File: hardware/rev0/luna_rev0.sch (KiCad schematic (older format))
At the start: 35 parts, among them J1 USB_B_Micro, J2 USB_B_Micro, J3 USB_A, J4 USB_B_Micro, J7 Conn_02x02_Counter_Clockwise, J8 Conn_Coaxial, J9 Conn_Coaxial, SW1 BTN_RECOVERY, SW2 BTN_DFU, SW3 BTN_RESET, U1 AP22814-SOT, U12 AP22814-SOT, Y1 DSC60xx

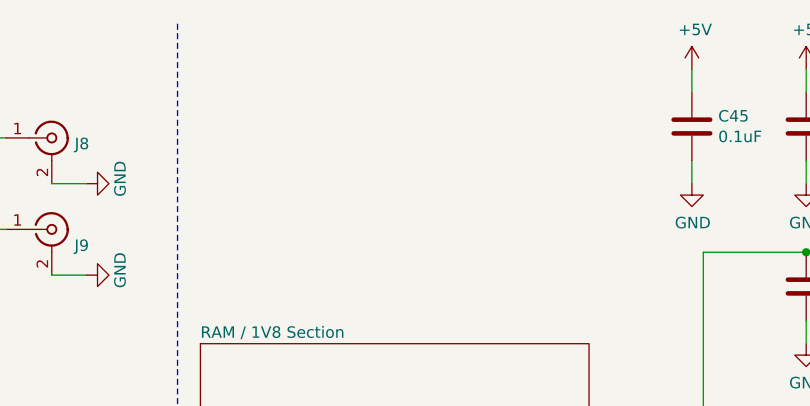
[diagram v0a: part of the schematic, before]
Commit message: hardware: add component selection notes
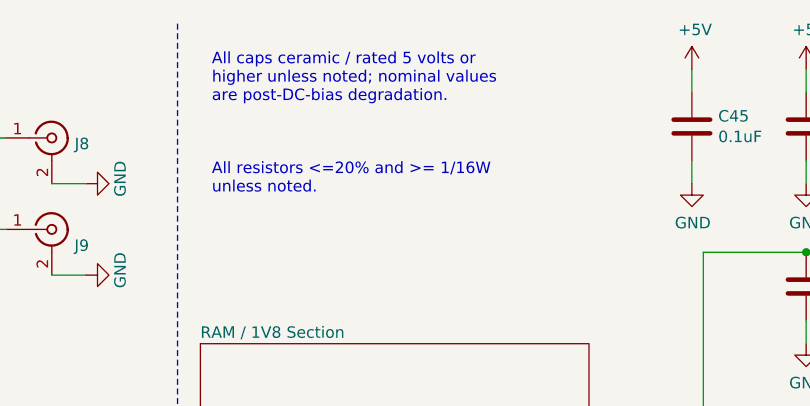
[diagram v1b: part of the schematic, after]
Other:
- note added: "All caps ceramic / rated 5 volts or\nhigher unless noted; nominal values\nare post-DC-bias degradation."
- note added: "All resistors <=20% and >= 1/16W\nunless noted."
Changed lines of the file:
@@
 Wire Wire Line
 	6150 700  6150 800
+Text Notes 4050 850  0    50   ~ 0
+All caps ceramic / rated 5 volts or\nhigher unless noted; nominal values\nare post-DC-bias degradation.
+Text Notes 4050 1250 0    50   ~ 0
+All resistors <=20% and >= 1/16W\nunless noted.
 $EndSCHEMATC

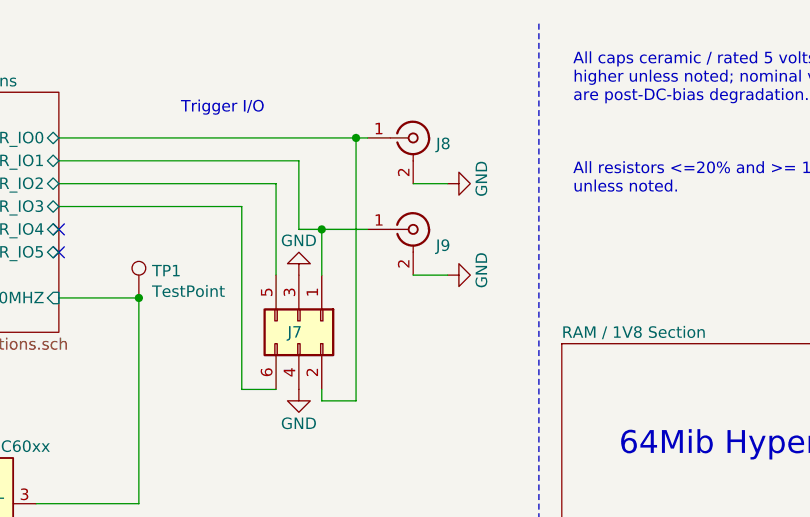
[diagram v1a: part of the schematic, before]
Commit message: hardware: do not populate J7-J9
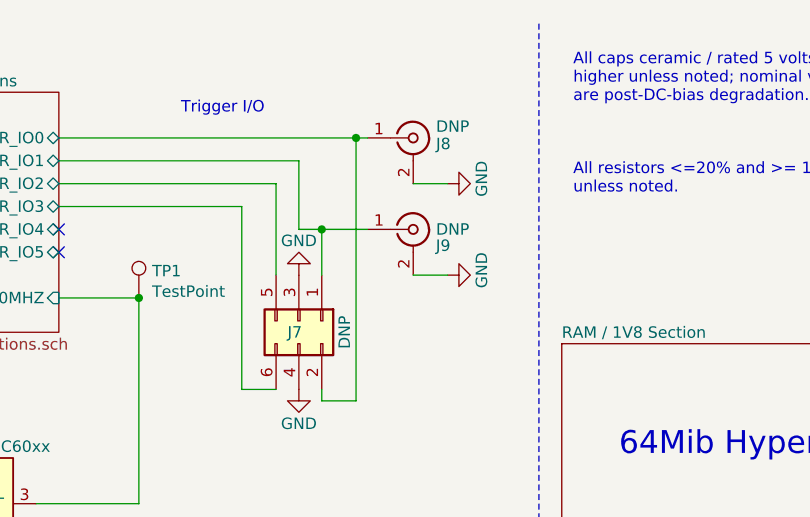
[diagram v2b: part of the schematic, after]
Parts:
- J7, J8, J9: Note (none) -> DNP
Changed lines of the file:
@@
 F 2 "luna:SMA-EDGE" H 3350 1000 50  0001 C CNN
 F 3 " ~" H 3350 1000 50  0001 C CNN
+F 4 "DNP" H 3450 1050 50  0000 L CNN "Note"
 	1    3350 1000
 	1    0    0    -1
@@
 F 2 "Connector_PinHeader_2.54mm:PinHeader_2x03_P2.54mm_Horizontal" H 2850 1800 50  0001 C CNN
 F 3 "~" H 2850 1800 50  0001 C CNN
+F 4 "DNP" H 2900 2000 50  0000 C CNN "Note"
 	1    2850 1800
 	0    1    1    0
@@
 F 2 "luna:SMA-EDGE" H 3350 1400 50  0001 C CNN
 F 3 " ~" H 3350 1400 50  0001 C CNN
+F 4 "DNP" H 3450 1400 50  0000 L CNN "Note"
 	1    3350 1400
 	1    0    0    -1
